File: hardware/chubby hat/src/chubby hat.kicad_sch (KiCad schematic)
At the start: 20 parts, among them J13 Conn_ARM_JTAG_SWD_10, J15 5V, J16 5V, J17 5V, J18 5V, J19 5V, J20 Conn_ARM_JTAG_SWD_10, J21 TC2030, U4 AMS1117-3.3

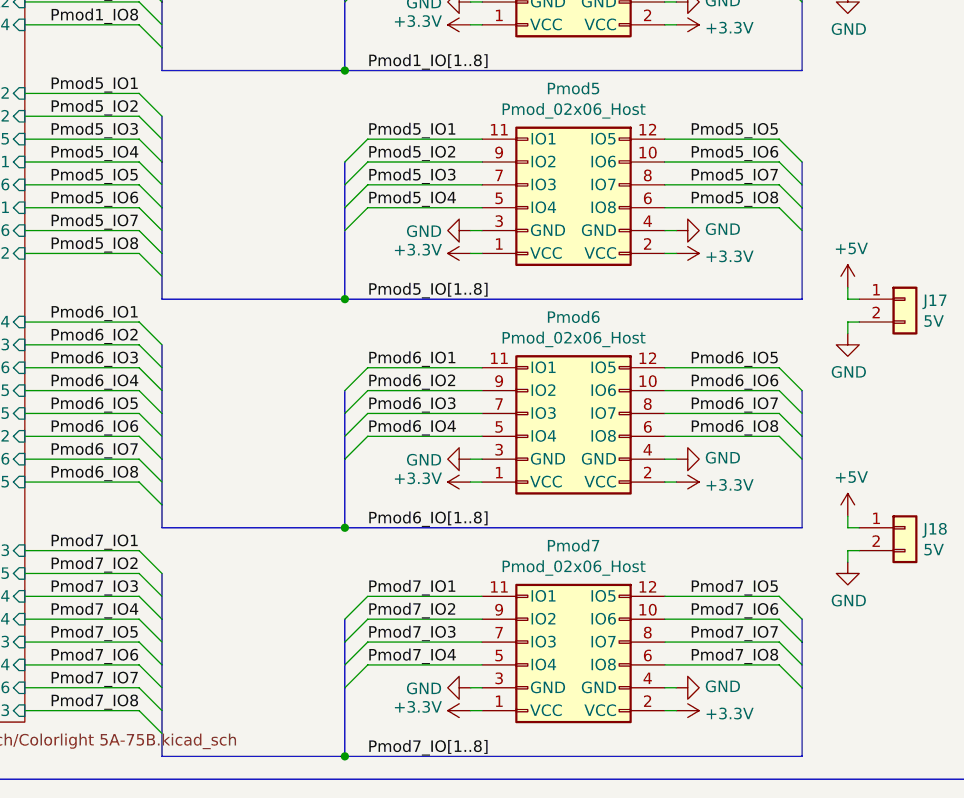
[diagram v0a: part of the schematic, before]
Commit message: fix STM32 USB; closes #2
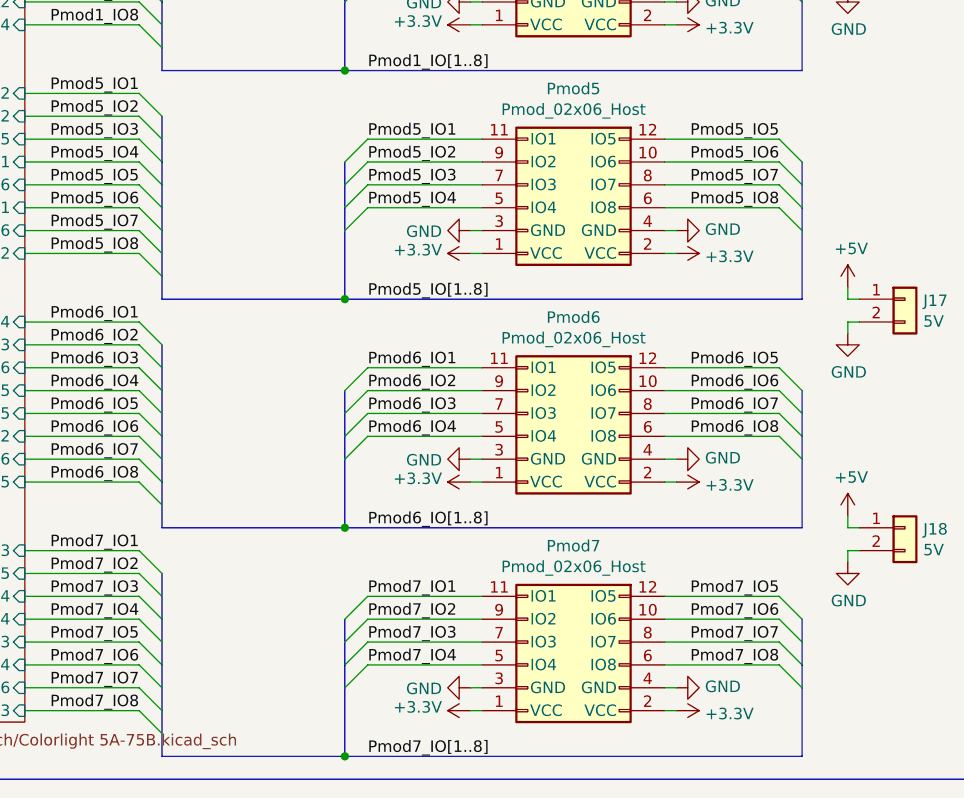
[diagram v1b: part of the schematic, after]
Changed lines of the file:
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@@
   (junction (at 281.94 190.5) (diameter 0) (color 0 0 0 0))
   (junction (at 281.94 215.9) (diameter 0) (color 0 0 0 0))
+  (no_connect (at 175.26 101.6))
   (no_connect (at 175.26 147.32))
-  (no_connect (at 175.26 101.6))
   (bus_entry (at 121.92 60.96) (size -2.54 -2.54)
     (stroke (width 0.1524) (type solid) (color 0 0 0 0))
@@
     (stroke (width 0) (type solid) (color 0 0 0 0))
   )
-  (bus (pts (xy 261.62 149.86) (xy 261.62 154.94))
-    (stroke (width 0) (type solid) (color 0 0 0 0))
-  )
-  (bus (pts (xy 261.62 154.94) (xy 261.62 160.02))
-    (stroke (width 0) (type solid) (color 0 0 0 0))
-  )
-  (bus (pts (xy 261.62 160.02) (xy 261.62 165.1))
+  (bus (pts (xy 261.62 149.86) (xy 261.62 152.4))
+    (stroke (width 0) (type solid) (color 0 0 0 0))
+  )
+  (bus (pts (xy 261.62 152.4) (xy 261.62 157.48))
+    (stroke (width 0) (type solid) (color 0 0 0 0))
+  )
+  (bus (pts (xy 261.62 157.48) (xy 261.62 162.56))
+    (stroke (width 0) (type solid) (color 0 0 0 0))
+  )
+  (bus (pts (xy 261.62 162.56) (xy 261.62 165.1))
     (stroke (width 0) (type solid) (color 0 0 0 0))
   )
@@
     (stroke (width 0) (type solid) (color 0 0 0 0))
   )
-  (bus (pts (xy 261.62 175.26) (xy 261.62 177.8))
-    (stroke (width 0) (type solid) (color 0 0 0 0))
-  )
-  (bus (pts (xy 261.62 177.8) (xy 261.62 182.88))
-    (stroke (width 0) (type solid) (color 0 0 0 0))
-  )
-  (bus (pts (xy 261.62 182.88) (xy 261.62 187.96))
-    (stroke (width 0) (type solid) (color 0 0 0 0))
-  )
-  (bus (pts (xy 261.62 187.96) (xy 261.62 190.5))
+  (bus (pts (xy 261.62 175.26) (xy 261.62 180.34))
+    (stroke (width 0) (type solid) (color 0 0 0 0))
+  )
+  (bus (pts (xy 261.62 180.34) (xy 261.62 185.42))
+    (stroke (width 0) (type solid) (color 0 0 0 0))
+  )
+  (bus (pts (xy 261.62 185.42) (xy 261.62 190.5))
     (stroke (width 0) (type solid) (color 0 0 0 0))
   )
@@
     (stroke (width 0) (type solid) (color 0 0 0 0))
   )
-  (bus (pts (xy 281.94 175.26) (xy 281.94 177.8))
-    (stroke (width 0) (type solid) (color 0 0 0 0))
-  )
-  (bus (pts (xy 281.94 177.8) (xy 281.94 182.88))
-    (stroke (width 0) (type solid) (color 0 0 0 0))
-  )
-  (bus (pts (xy 281.94 182.88) (xy 281.94 190.5))
+  (bus (pts (xy 281.94 175.26) (xy 281.94 180.34))
+    (stroke (width 0) (type solid) (color 0 0 0 0))
+  )
+  (bus (pts (xy 281.94 180.34) (xy 281.94 190.5))
     (stroke (width 0) (type solid) (color 0 0 0 0))
   )
@@
     (stroke (width 0) (type solid) (color 0 0 0 0))
   )
-  (bus (pts (xy 281.94 200.66) (xy 281.94 203.2))
-    (stroke (width 0) (type solid) (color 0 0 0 0))
-  )
-  (bus (pts (xy 281.94 203.2) (xy 281.94 208.28))
-    (stroke (width 0) (type solid) (color 0 0 0 0))
-  )
-  (bus (pts (xy 281.94 208.28) (xy 281.94 215.9))
+  (bus (pts (xy 281.94 200.66) (xy 281.94 205.74))
+    (stroke (width 0) (type solid) (color 0 0 0 0))
+  )
+  (bus (pts (xy 281.94 205.74) (xy 281.94 215.9))
     (stroke (width 0) (type solid) (color 0 0 0 0))
   )
@@
     (stroke (width 0) (type solid) (color 0 0 0 0))
   )
-  (bus (pts (xy 332.74 200.66) (xy 332.74 203.2))
-    (stroke (width 0) (type solid) (color 0 0 0 0))
-  )
-  (bus (pts (xy 332.74 203.2) (xy 332.74 208.28))
-    (stroke (width 0) (type solid) (color 0 0 0 0))
-  )
-  (bus (pts (xy 332.74 208.28) (xy 332.74 215.9))
-    (stroke (width 0) (type solid) (color 0 0 0 0))
-  )
+  (bus (pts (xy 332.74 200.66) (xy 332.74 205.74))
+    (stroke (width 0) (type solid) (color 0 0 0 0))
+  )
+  (bus (pts (xy 332.74 205.74) (xy 332.74 215.9))
+    (stroke (width 0) (type solid) (color 0 0 0 0))
+  )

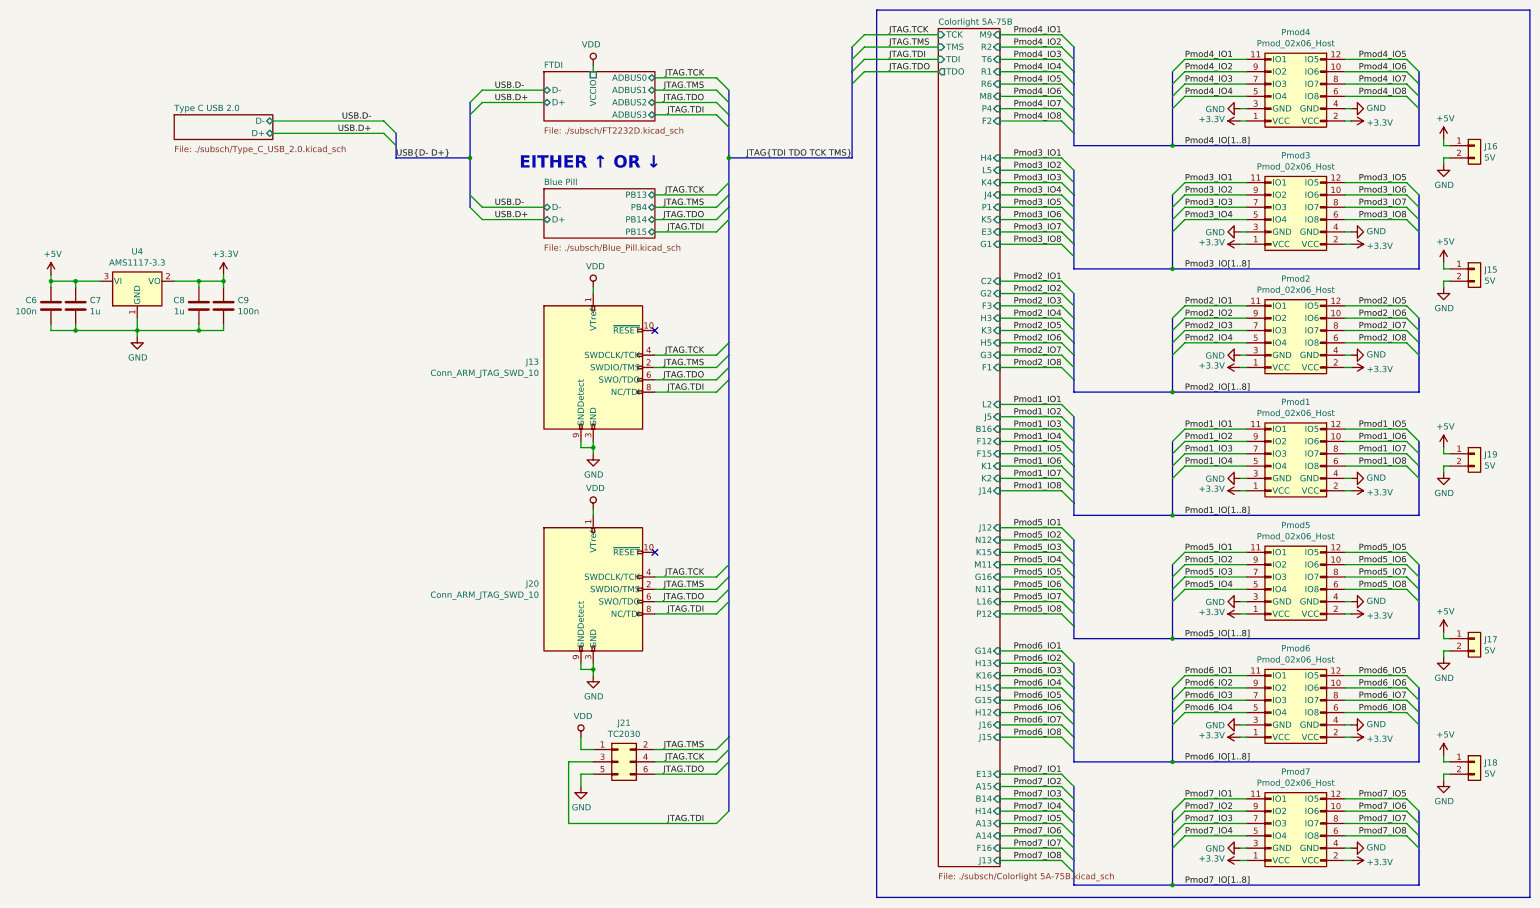
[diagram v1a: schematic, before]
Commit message: fixed wrong JTAG signal assignment on FTDI
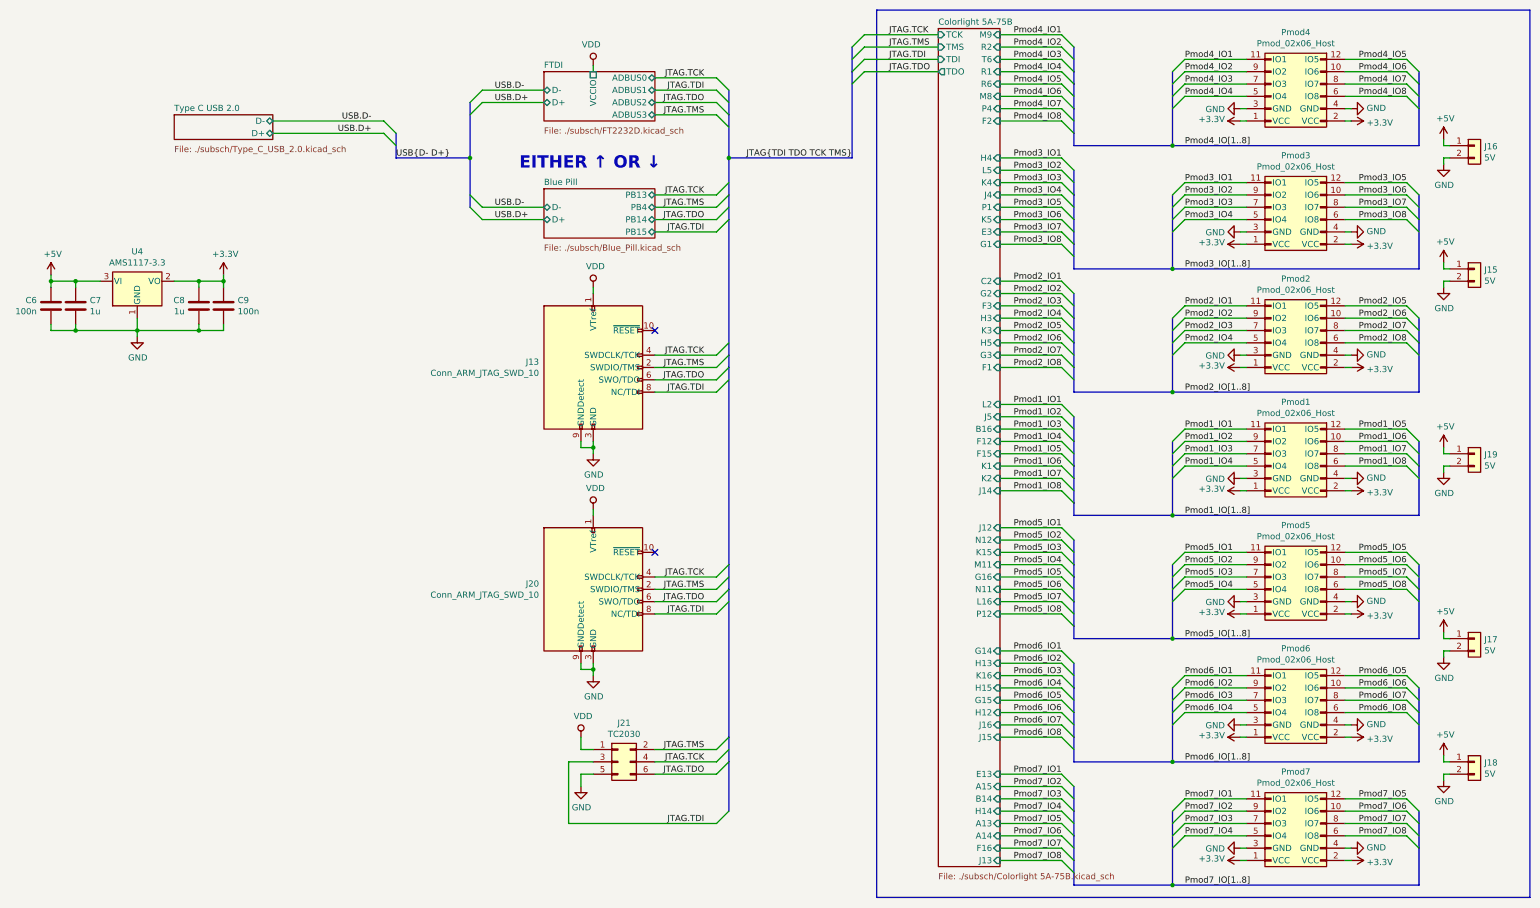
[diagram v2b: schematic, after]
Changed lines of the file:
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@@
     (stroke (width 0) (type solid) (color 0 0 0 0))
   )
-  (bus (pts (xy 190.5 73.66) (xy 190.5 76.2))
-    (stroke (width 0) (type solid) (color 0 0 0 0))
-  )
-  (bus (pts (xy 190.5 76.2) (xy 190.5 104.14))
-    (stroke (width 0) (type solid) (color 0 0 0 0))
-  )
-  (bus (pts (xy 190.5 104.14) (xy 190.5 106.68))
-    (stroke (width 0) (type solid) (color 0 0 0 0))
-  )
-  (bus (pts (xy 190.5 106.68) (xy 190.5 111.76))
-    (stroke (width 0) (type solid) (color 0 0 0 0))
-  )
-  (bus (pts (xy 190.5 111.76) (xy 190.5 152.4))
-    (stroke (width 0) (type solid) (color 0 0 0 0))
-  )
-  (bus (pts (xy 190.5 152.4) (xy 190.5 157.48))
-    (stroke (width 0) (type solid) (color 0 0 0 0))
-  )
-  (bus (pts (xy 190.5 157.48) (xy 190.5 185.42))
+  (bus (pts (xy 190.5 73.66) (xy 190.5 78.74))
+    (stroke (width 0) (type solid) (color 0 0 0 0))
+  )
+  (bus (pts (xy 190.5 78.74) (xy 190.5 106.68))
+    (stroke (width 0) (type solid) (color 0 0 0 0))
+  )
+  (bus (pts (xy 190.5 106.68) (xy 190.5 109.22))
+    (stroke (width 0) (type solid) (color 0 0 0 0))
+  )
+  (bus (pts (xy 190.5 109.22) (xy 190.5 149.86))
+    (stroke (width 0) (type solid) (color 0 0 0 0))
+  )
+  (bus (pts (xy 190.5 149.86) (xy 190.5 154.94))
+    (stroke (width 0) (type solid) (color 0 0 0 0))
+  )
+  (bus (pts (xy 190.5 154.94) (xy 190.5 185.42))
     (stroke (width 0) (type solid) (color 0 0 0 0))
   )
@@
     (stroke (width 0) (type solid) (color 0 0 0 0))
   )
-  (bus (pts (xy 261.62 104.14) (xy 261.62 106.68))
-    (stroke (width 0) (type solid) (color 0 0 0 0))
-  )
-  (bus (pts (xy 261.62 106.68) (xy 261.62 111.76))
-    (stroke (width 0) (type solid) (color 0 0 0 0))
-  )
-  (bus (pts (xy 261.62 111.76) (xy 261.62 114.3))
+  (bus (pts (xy 261.62 104.14) (xy 261.62 109.22))
+    (stroke (width 0) (type solid) (color 0 0 0 0))
+  )
+  (bus (pts (xy 261.62 109.22) (xy 261.62 114.3))
     (stroke (width 0) (type solid) (color 0 0 0 0))
   )
@@
     (stroke (width 0) (type solid) (color 0 0 0 0))
   )
-  (bus (pts (xy 281.94 200.66) (xy 281.94 205.74))
-    (stroke (width 0) (type solid) (color 0 0 0 0))
-  )
-  (bus (pts (xy 281.94 205.74) (xy 281.94 215.9))
+  (bus (pts (xy 281.94 200.66) (xy 281.94 203.2))
+    (stroke (width 0) (type solid) (color 0 0 0 0))
+  )
+  (bus (pts (xy 281.94 203.2) (xy 281.94 208.28))
+    (stroke (width 0) (type solid) (color 0 0 0 0))
+  )
+  (bus (pts (xy 281.94 208.28) (xy 281.94 215.9))
     (stroke (width 0) (type solid) (color 0 0 0 0))
   )
@@
     (stroke (width 0) (type solid) (color 0 0 0 0))
   )
-  (bus (pts (xy 332.74 200.66) (xy 332.74 205.74))
-    (stroke (width 0) (type solid) (color 0 0 0 0))
-  )
-  (bus (pts (xy 332.74 205.74) (xy 332.74 215.9))
+  (bus (pts (xy 332.74 200.66) (xy 332.74 203.2))
+    (stroke (width 0) (type solid) (color 0 0 0 0))
+  )
+  (bus (pts (xy 332.74 203.2) (xy 332.74 208.28))
+    (stroke (width 0) (type solid) (color 0 0 0 0))
+  )
+  (bus (pts (xy 332.74 208.28) (xy 332.74 215.9))
     (stroke (width 0) (type solid) (color 0 0 0 0))
   )
@@
     (effects (font (size 1.27 1.27)) (justify right bottom))
   )
-  (label "JTAG.TMS" (at 185.42 52.07 180)
+  (label "JTAG.TDI" (at 185.42 52.07 180)
     (effects (font (size 1.27 1.27)) (justify right bottom))
   )
@@
     (effects (font (size 1.27 1.27)) (justify right bottom))
   )
-  (label "JTAG.TDI" (at 185.42 57.15 180)
-    (effects (font (size 1.27 1.27)) (justify right bottom))
-  )
+  (label "JTAG.TMS" (at 185.42 57.15 180)
+    (effects (font (size 1.27 1.27)) (justify right bottom))
+  )
